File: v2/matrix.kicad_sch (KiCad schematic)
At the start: 136 parts, among them SW10 KC_7, SW11 KC_8, SW12 KC_9, SW13 KC_0, SW14 KC_MINUS, SW15 KC_EQUAL, SW16 KC_BACKSPACE, SW17 KC_TAB, SW18 KC_Q, SW19 KC_W, SW20 KC_E, SW21 KC_R, SW22 KC_T, SW23 KC_Y, SW24 KC_U, SW25 KC_I, SW26 KC_O, SW27 KC_P, SW28 KC_LEFT_BRACKET, SW29 KC_RIGHT_BRACKET, SW3 KC_ESCAPE, SW30 KC_DEL, SW31 KC_CAPS, SW32 KC_A, SW33 KC_S, SW34 KC_D, SW35 KC_F, SW36 KC_G, SW37 KC_H, SW38 KC_J, SW39 KC_K, SW4 KC_1, SW40 KC_L, SW41 KC_SEMICOLON, SW42 KC_QUOTE, SW43 KC_NONUS_HASH, SW44 KC_ENTER, SW45 KC_PAGE_UP, SW46 KC_LEFT_SHIFT, SW47 KC_GRAVE, SW48 KC_Z, SW49 KC_X, SW5 KC_2, SW50 KC_C, SW51 KC_V, SW52 KC_B, SW53 KC_N, SW54 KC_M, SW55 KC_COMMA, SW56 KC_DOT, SW57 KC_SLASH, SW58 KC_RIGHT_SHIFT, SW59 KC_UP, SW6 KC_3, SW60 KC_PAGE_DOWN, SW61 KC_LEFT_CTRL, SW62 KC_LEFT_GUI, SW63 KC_LEFT_ALT, SW64 KC_SPACE, SW65 KC_RIGHT_ALT, SW66 KC_RIGHT_GUI, SW67 KC_RIGHT_CTRL, SW68 KC_LEFT, SW69 KC_DOWN, SW7 KC_4, SW70 KC_RIGHT, SW8 KC_5, SW9 KC_6

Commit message: First try at manufacturing files
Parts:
- SW10, SW11, SW12, SW13, SW14, SW15, SW16, SW17, SW18, SW19, SW20, SW21, SW22, SW23, SW24, SW25, SW26, SW27, SW28, SW29, SW3, SW30, SW31, SW32, SW33, SW34, SW35, SW36, SW37, SW38, SW39, SW4, SW40, SW41, SW42, SW43, SW44, SW45, SW46, SW47, SW48, SW49, SW5, SW50, SW51, SW52, SW53, SW54, SW55, SW56, SW57, SW58, SW59, SW6, SW60, SW61, SW62, SW63, SW64, SW65, SW66, SW67, SW68, SW69, SW7, SW70, SW8, SW9: now left out of the parts list
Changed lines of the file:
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@@
 		(unit 1)
 		(exclude_from_sim no)
-		(in_bom yes)
+		(in_bom no)
 		(on_board yes)
 		(dnp no)
@@
 		(unit 1)
 		(exclude_from_sim no)
-		(in_bom yes)
+		(in_bom no)
 		(on_board yes)
 		(dnp no)
@@
 		(unit 1)
 		(exclude_from_sim no)
-		(in_bom yes)
+		(in_bom no)
 		(on_board yes)
 		(dnp no)
@@
 		(unit 1)
 		(exclude_from_sim no)
-		(in_bom yes)
+		(in_bom no)
 		(on_board yes)
 		(dnp no)
@@
 		(unit 1)
 		(exclude_from_sim no)
-		(in_bom yes)
+		(in_bom no)
 		(on_board yes)
 		(dnp no)
@@
 		(unit 1)
 		(exclude_from_sim no)
-		(in_bom yes)
+		(in_bom no)
 		(on_board yes)
 		(dnp no)
@@
 		(unit 1)
 		(exclude_from_sim no)
-		(in_bom yes)
+		(in_bom no)
 		(on_board yes)
 		(dnp no)
@@
 		(unit 1)
 		(exclude_from_sim no)
-		(in_bom yes)
+		(in_bom no)
 		(on_board yes)
 		(dnp no)
@@
 		(unit 1)
 		(exclude_from_sim no)
-		(in_bom yes)
+		(in_bom no)
 		(on_board yes)
 		(dnp no)
@@
 		(unit 1)
 		(exclude_from_sim no)
-		(in_bom yes)
+		(in_bom no)
 		(on_board yes)
 		(dnp no)
@@
 		(unit 1)
 		(exclude_from_sim no)
-		(in_bom yes)
+		(in_bom no)
 		(on_board yes)
 		(dnp no)
@@
 		(unit 1)
 		(exclude_from_sim no)
-		(in_bom yes)
+		(in_bom no)
 		(on_board yes)
 		(dnp no)
@@
 		(unit 1)
 		(exclude_from_sim no)
-		(in_bom yes)
+		(in_bom no)
 		(on_board yes)
 		(dnp no)
@@
 		(unit 1)
 		(exclude_from_sim no)
-		(in_bom yes)
+		(in_bom no)
 		(on_board yes)
 		(dnp no)
@@
 		(unit 1)
 		(exclude_from_sim no)
-		(in_bom yes)
+		(in_bom no)
 		(on_board yes)
 		(dnp no)
@@
 		(unit 1)
 		(exclude_from_sim no)
-		(in_bom yes)
+		(in_bom no)
 		(on_board yes)
 		(dnp no)
@@
 		(unit 1)
 		(exclude_from_sim no)
-		(in_bom yes)
+		(in_bom no)
 		(on_board yes)
 		(dnp no)
@@
 		(unit 1)
 		(exclude_from_sim no)
-		(in_bom yes)
+		(in_bom no)
 		(on_board yes)
 		(dnp no)
@@
 		(unit 1)
 		(exclude_from_sim no)
-		(in_bom yes)
+		(in_bom no)
 		(on_board yes)
 		(dnp no)
@@
 		(unit 1)
 		(exclude_from_sim no)
-		(in_bom yes)
+		(in_bom no)
 		(on_board yes)
 		(dnp no)
@@
 		(unit 1)
 		(exclude_from_sim no)
-		(in_bom yes)
+		(in_bom no)
 		(on_board yes)
 		(dnp no)
@@
 		(unit 1)
 		(exclude_from_sim no)
-		(in_bom yes)
+		(in_bom no)
 		(on_board yes)
 		(dnp no)
@@
 		(unit 1)
 		(exclude_from_sim no)
-		(in_bom yes)
+		(in_bom no)
 		(on_board yes)
 		(dnp no)
@@
 		(unit 1)
 		(exclude_from_sim no)
-		(in_bom yes)
+		(in_bom no)
 		(on_board yes)
 		(dnp no)
@@
 		(unit 1)
 		(exclude_from_sim no)
-		(in_bom yes)
+		(in_bom no)
 		(on_board yes)
 		(dnp no)
@@
 		(unit 1)
 		(exclude_from_sim no)
-		(in_bom yes)
+		(in_bom no)
 		(on_board yes)
 		(dnp no)
@@
 		(unit 1)
 		(exclude_from_sim no)
-		(in_bom yes)
+		(in_bom no)
 		(on_board yes)
 		(dnp no)
@@
 		(unit 1)
 		(exclude_from_sim no)
-		(in_bom yes)
+		(in_bom no)
 		(on_board yes)
 		(dnp no)
@@
 		(unit 1)
 		(exclude_from_sim no)
-		(in_bom yes)
+		(in_bom no)
 		(on_board yes)
 		(dnp no)
@@
 		(unit 1)
 		(exclude_from_sim no)
-		(in_bom yes)
+		(in_bom no)
 		(on_board yes)
 		(dnp no)
@@
 		(unit 1)
 		(exclude_from_sim no)
-		(in_bom yes)
+		(in_bom no)
 		(on_board yes)
 		(dnp no)
@@
 		(unit 1)
 		(exclude_from_sim no)
-		(in_bom yes)
+		(in_bom no)
 		(on_board yes)
 		(dnp no)
@@
 		(unit 1)
 		(exclude_from_sim no)
-		(in_bom yes)
+		(in_bom no)
 		(on_board yes)
 		(dnp no)
@@
 		(unit 1)
 		(exclude_from_sim no)
-		(in_bom yes)
+		(in_bom no)
 		(on_board yes)
 		(dnp no)
@@
 		(unit 1)
 		(exclude_from_sim no)
-		(in_bom yes)
+		(in_bom no)
 		(on_board yes)
 		(dnp no)
@@
 		(unit 1)
 		(exclude_from_sim no)
-		(in_bom yes)
+		(in_bom no)
 		(on_board yes)
 		(dnp no)
@@
 		(unit 1)
 		(exclude_from_sim no)
-		(in_bom yes)
+		(in_bom no)
 		(on_board yes)
 		(dnp no)
@@
 		(unit 1)
 		(exclude_from_sim no)
-		(in_bom yes)
+		(in_bom no)
 		(on_board yes)
 		(dnp no)
@@
 		(unit 1)
 		(exclude_from_sim no)
-		(in_bom yes)
+		(in_bom no)
 		(on_board yes)
 		(dnp no)
@@
 		(unit 1)
 		(exclude_from_sim no)
-		(in_bom yes)
+		(in_bom no)
 		(on_board yes)
 		(dnp no)
@@
 		(unit 1)
 		(exclude_from_sim no)
-		(in_bom yes)
+		(in_bom no)
 		(on_board yes)
 		(dnp no)
@@
 		(unit 1)
 		(exclude_from_sim no)
-		(in_bom yes)
+		(in_bom no)
 		(on_board yes)
 		(dnp no)
@@
 		(unit 1)
 		(exclude_from_sim no)
-		(in_bom yes)
+		(in_bom no)
 		(on_board yes)
 		(dnp no)
@@
 		(unit 1)
 		(exclude_from_sim no)
-		(in_bom yes)
+		(in_bom no)
 		(on_board yes)
 		(dnp no)
@@
 		(unit 1)
 		(exclude_from_sim no)
-		(in_bom yes)
+		(in_bom no)
 		(on_board yes)
 		(dnp no)
@@
 		(unit 1)
 		(exclude_from_sim no)
-		(in_bom yes)
+		(in_bom no)
 		(on_board yes)
 		(dnp no)
@@
 		(unit 1)
 		(exclude_from_sim no)
-		(in_bom yes)
+		(in_bom no)
 		(on_board yes)
 		(dnp no)
@@
 		(unit 1)
 		(exclude_from_sim no)
-		(in_bom yes)
+		(in_bom no)
 		(on_board yes)
 		(dnp no)
@@
 		(unit 1)
 		(exclude_from_sim no)
-		(in_bom yes)
+		(in_bom no)
 		(on_board yes)
 		(dnp no)
@@
 		(unit 1)
 		(exclude_from_sim no)
-		(in_bom yes)
+		(in_bom no)
 		(on_board yes)
 		(dnp no)
@@
 		(unit 1)
 		(exclude_from_sim no)
-		(in_bom yes)
+		(in_bom no)
 		(on_board yes)
 		(dnp no)
@@
 		(unit 1)
 		(exclude_from_sim no)
-		(in_bom yes)
+		(in_bom no)
 		(on_board yes)
 		(dnp no)
@@
 		(unit 1)
 		(exclude_from_sim no)
-		(in_bom yes)
+		(in_bom no)
 		(on_board yes)
 		(dnp no)
@@
 		(unit 1)
 		(exclude_from_sim no)
-		(in_bom yes)
+		(in_bom no)
 		(on_board yes)
 		(dnp no)
@@
 		(unit 1)
 		(exclude_from_sim no)
-		(in_bom yes)
+		(in_bom no)
 		(on_board yes)
 		(dnp no)
@@
 		(unit 1)
 		(exclude_from_sim no)
-		(in_bom yes)
+		(in_bom no)
 		(on_board yes)
 		(dnp no)
@@
 		(unit 1)
 		(exclude_from_sim no)
-		(in_bom yes)
+		(in_bom no)
 		(on_board yes)
 		(dnp no)
@@
 		(unit 1)
 		(exclude_from_sim no)
-		(in_bom yes)
+		(in_bom no)
 		(on_board yes)
 		(dnp no)
@@
 		(unit 1)
 		(exclude_from_sim no)
-		(in_bom yes)
+		(in_bom no)
 		(on_board yes)
 		(dnp no)
@@
 		(unit 1)
 		(exclude_from_sim no)
-		(in_bom yes)
+		(in_bom no)
 		(on_board yes)
 		(dnp no)
@@
 		(unit 1)
 		(exclude_from_sim no)
-		(in_bom yes)
+		(in_bom no)
 		(on_board yes)
 		(dnp no)
@@
 		(unit 1)
 		(exclude_from_sim no)
-		(in_bom yes)
+		(in_bom no)
 		(on_board yes)
 		(dnp no)
@@
 		(unit 1)
 		(exclude_from_sim no)
-		(in_bom yes)
+		(in_bom no)
 		(on_board yes)
 		(dnp no)
@@
 		(unit 1)
 		(exclude_from_sim no)
-		(in_bom yes)
+		(in_bom no)
 		(on_board yes)
 		(dnp no)
@@
 		(unit 1)
 		(exclude_from_sim no)
-		(in_bom yes)
+		(in_bom no)
 		(on_board yes)
 		(dnp no)
@@
 		(unit 1)
 		(exclude_from_sim no)
-		(in_bom yes)
+		(in_bom no)
 		(on_board yes)
 		(dnp no)
@@
 		(unit 1)
 		(exclude_from_sim no)
-		(in_bom yes)
+		(in_bom no)
 		(on_board yes)
 		(dnp no)
@@
 		(unit 1)
 		(exclude_from_sim no)
-		(in_bom yes)
+		(in_bom no)
 		(on_board yes)
 		(dnp no)

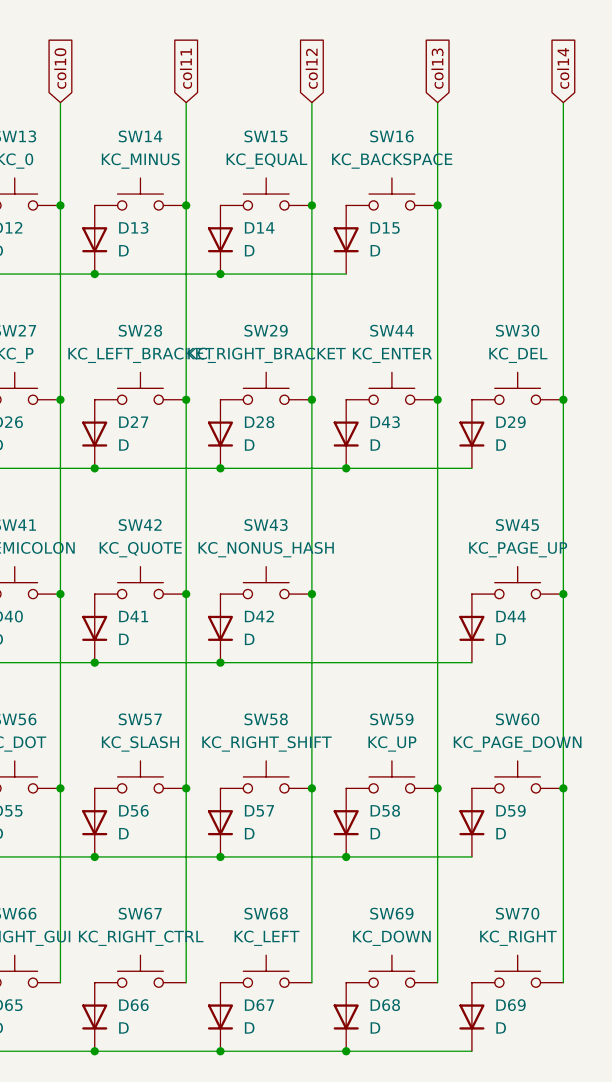
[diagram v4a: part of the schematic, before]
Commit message: squeeze keyboard in case
removed colomn 14 (4 keys), TTRS connection, and rotary encoder
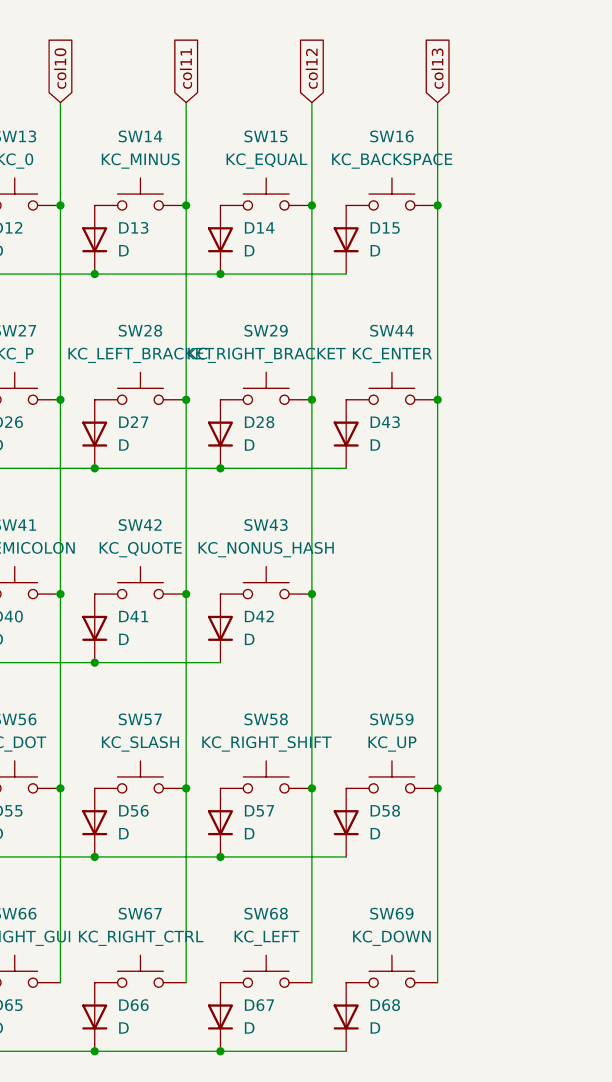
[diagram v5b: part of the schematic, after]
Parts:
- removed D29, D44, D59, D69: D, Diode_SMD:D_SOD-123, symbol Device:D
- removed SW30: KC_DEL, Button_Switch_Keyboard:SW_Cherry_MX_1.00u_PCB, symbol Switch:SW_Push
- removed SW45: KC_PAGE_UP, Button_Switch_Keyboard:SW_Cherry_MX_1.00u_PCB, symbol Switch:SW_Push
- removed SW60: KC_PAGE_DOWN, Button_Switch_Keyboard:SW_Cherry_MX_1.00u_PCB, symbol Switch:SW_Push
- removed SW70: KC_RIGHT, Button_Switch_Keyboard:SW_Cherry_MX_1.00u_PCB, symbol Switch:SW_Push
